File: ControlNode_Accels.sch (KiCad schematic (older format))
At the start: 9 parts

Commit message: Update height sensors.
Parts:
- U? (x3): symbol MMA8451Q -> MMA8451Q-RESCUE-Control_Board
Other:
- moved on the sheet: U?
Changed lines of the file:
@@
 Original Author: SafetyLok
 $Comp
-L MMA8451Q U?
+L MMA8451Q-RESCUE-Control_Board U?
 U 1 1 57550C5F
 P 6150 4000
@@
 $EndComp
 $Comp
-L MMA8451Q U?
+L MMA8451Q-RESCUE-Control_Board U?
 U 1 1 57550CF8
 P 6150 5600
@@
 $EndComp
 $Comp
-L MMA8451Q U?
+L MMA8451Q-RESCUE-Control_Board U?
 U 1 1 57550D59
 P 6150 7200

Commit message: Release 1
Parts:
- removed C? (x6): 100n, symbol C
- removed U? (x2): MMA8451Q, symbol MMA8451Q-RESCUE-Control_Board
- added C? (x6): C_100nF_50V, RLOOP_FOOTPRINTS:rLoop_C_0603, symbol C_100nF_50V
- added R? (x3): 10K, RLOOP_FOOTPRINTS:rLoop_R_0603, symbol 10K
- added U? (x2): MMA8451Q, RLOOP_FOOTPRINTS:rLoop_QFN16_3x3mm, symbol MMA8451Q
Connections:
- net ACCEL1_I2C_SCL: now also U?.4 (SCL), U?.4 (SCL)
- net ACCEL1_I2C_SDA: now also U?.6 (SDA), U?.6 (SDA)
- net ACCEL1_NINT: now also U?.11 (INT1)
- net ACCEL2_NINT: now also U?.11 (INT1)
- net +3V3: now reaches U?.1 (VDDIO)
- net +3V3: now also U?.14 (VDD), C?.1, C?.1, C?.1, R?.2, R?.2, R?.2, U?.1 (VDDIO), U?.1 (VDDIO), U?.14 (VDD), U?.14 (VDD), U?.7 (SA0)
- net GNDD: now reaches U?.10 (GND)
- net GNDD: now also U?.12 (GND), U?.5 (GND), U?.7 (SA0), C?.2, C?.2, C?.2, C?.2, C?.2, C?.2, U?.10 (GND), U?.10 (GND), U?.12 (GND), U?.12 (GND), U?.5 (GND), U?.5 (GND), U?.7 (SA0)
- net at U?.2 (BYP): now also C?.1
- new net: C?.1, U?.2 (BYP) (x2)

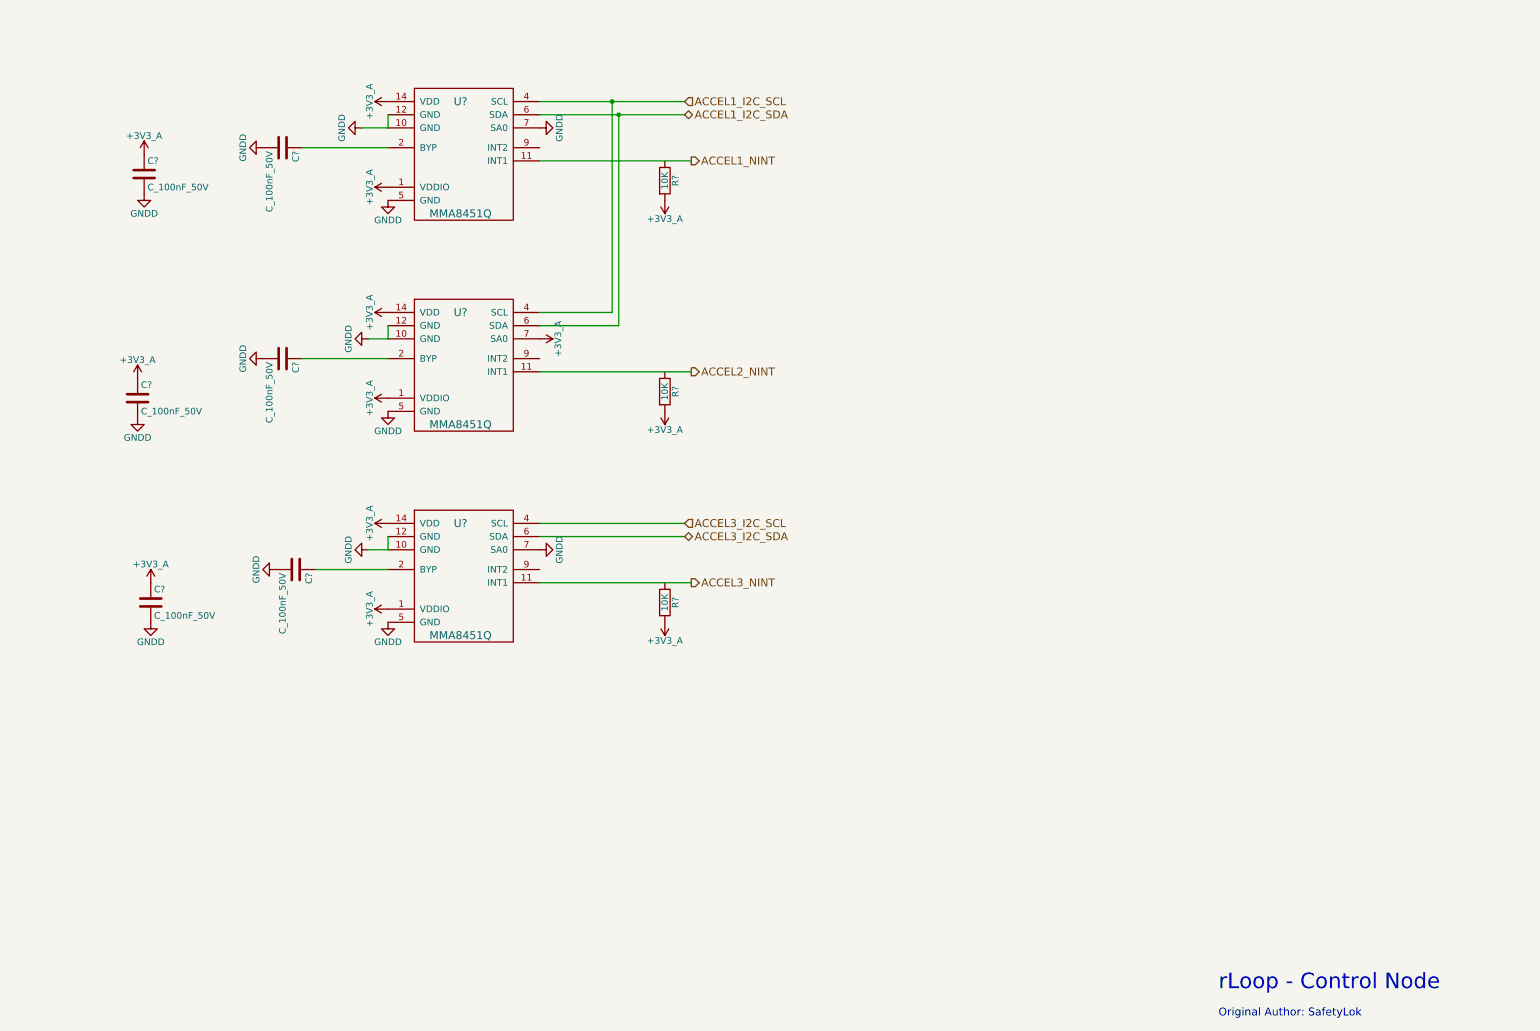
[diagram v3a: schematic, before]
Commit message: Update 10K pullups, 100R on RS422's and additional bypass caps.
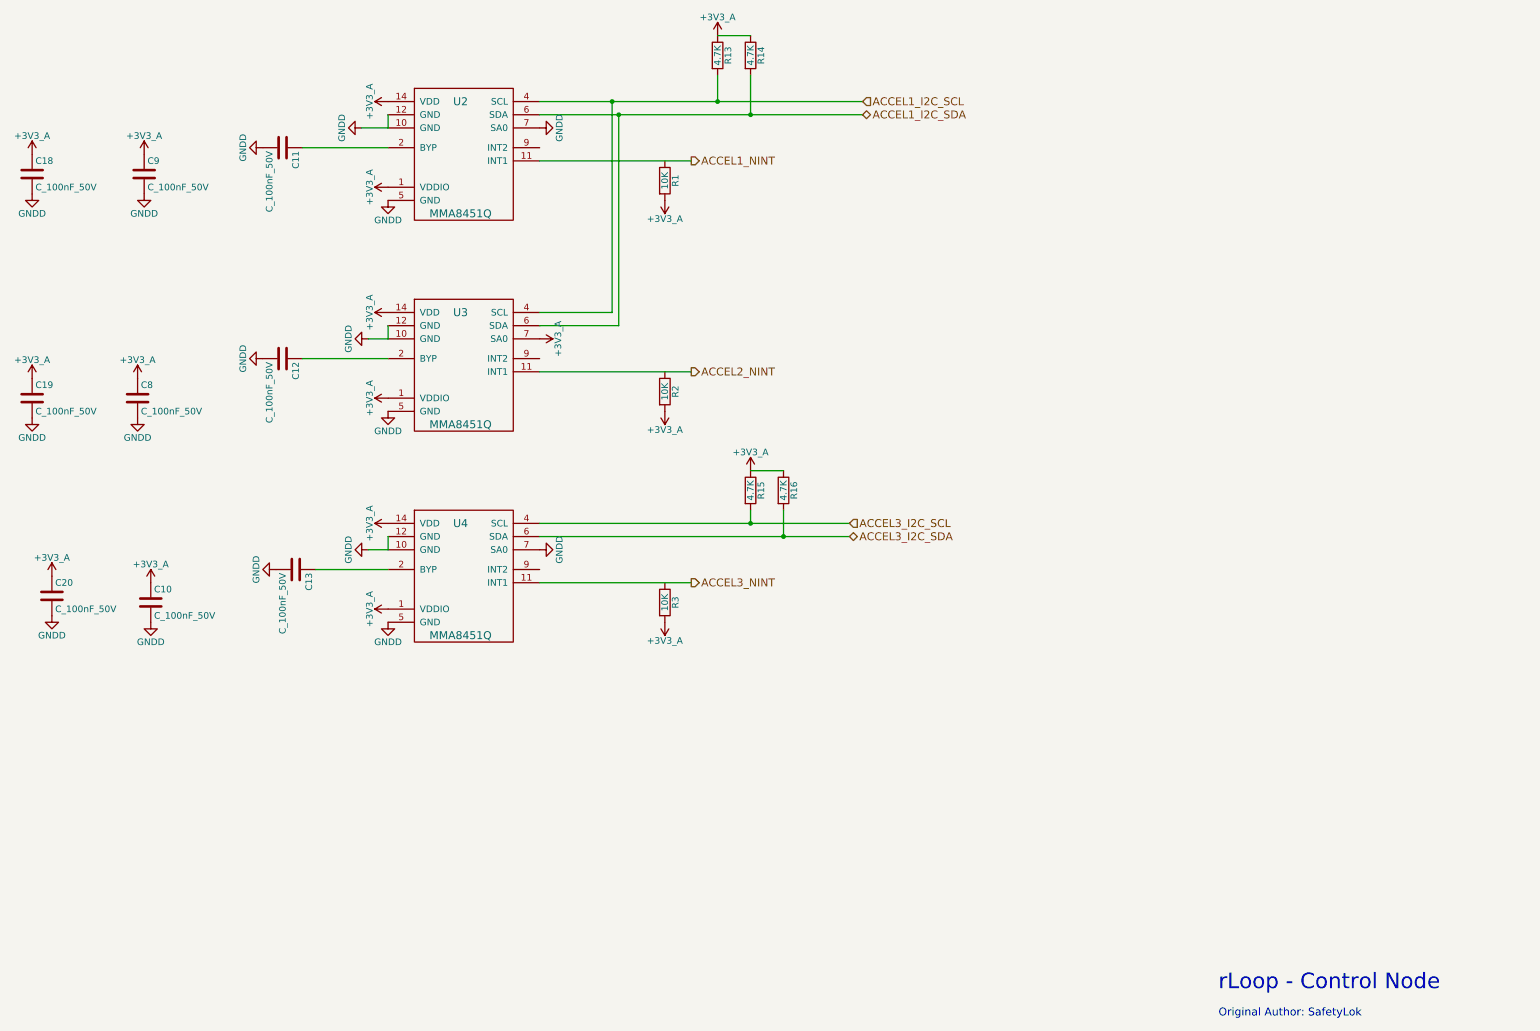
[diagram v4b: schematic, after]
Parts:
- added C18, C19, C20: C_100nF_50V, RLOOP_FOOTPRINTS:rLoop_C_0603, symbol C_100nF_50V
- added R13, R14, R15, R16: 4.7K, RLOOP_FOOTPRINTS:rLoop_R_0603, symbol 4.7K
- gave numbers to parts that had none: 12
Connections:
- net +3V3: now also C18.1, C19.1, C20.1, R13.1, R14.1, R15.1, R16.1
- net ACCEL1_I2C_SCL: now also R13.2
- net ACCEL1_I2C_SDA: now also R14.2
- net ACCEL3_I2C_SCL: now also R15.2
- net ACCEL3_I2C_SDA: now also R16.2
- net GNDD: now also C18.2, C19.2, C20.2
